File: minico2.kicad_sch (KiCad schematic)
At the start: 36 parts, among them J1 USB_C_Receptacle_USB2.0, J2 GDEY0213Z98, Q1 MMBT2222, Q2 MMBT2222, Q3 IRLML0100TRPBF, U1 ESP32-WROOM-32E, U2 CH340C, U3 TLV62568DBV, U5 SCD30

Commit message: Route PCB
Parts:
- removed C3: 6.8pF, Capacitor_SMD:C_0402_1005Metric, symbol Device:C_Small
- removed U3: TLV62568DBV, Package_TO_SOT_SMD:SOT-23-5, symbol Regulator_Switching:TLV62568DBV
- added H1, H2, H3, H4: MountingHole, MountingHole:MountingHole_2.7mm_M2.5, symbol Mechanical:MountingHole
- added TP1, TP2, TP3: TestPoint_Small, TestPoint:TestPoint_Pad_D2.0mm, symbol Connector:TestPoint_Small
- added TP4, TP5, TP6, TP7: TestPoint_Small, TestPoint:TestPoint_Pad_D1.0mm, symbol Connector:TestPoint_Small
- added U3: AP3418, minico2:SOT-25, symbol minico2:AP3418
- C1: value 10nF -> 100nF; footprint Capacitor_SMD:C_0402_1005Metric -> Capacitor_SMD:C_0603_1608Metric
- C2, C4, C7: footprint Capacitor_SMD:C_0402_1005Metric -> Capacitor_SMD:C_0603_1608Metric
- C9: value 1µF 25F -> 1µF 25V
- L2: footprint Inductor_SMD:L_1008_2520Metric -> Inductor_SMD:L_Taiyo-Yuden_NR-60xx
- R10, R4, R9: footprint Resistor_SMD:R_0402_1005Metric -> Resistor_SMD:R_0603_1608Metric
- R3: value 450kΩ -> 453kΩ; footprint Resistor_SMD:R_0402_1005Metric -> Resistor_SMD:R_0603_1608Metric
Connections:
- net +3V3: now also TP3.1; no longer U2.16 (VCC)
- net +5V: now also U2.16 (VCC), TP2.1, U3.1 (EN), U3.4 (VIN)
- net EN: now also TP5.1
- net ESP_RX: now also TP7.1
- net ESP_TX: now also TP6.1
- net GND: now also TP1.1, U3.2 (GND)
- net GPIO0: now also TP4.1
- net at R3.2, R4.1: now also U3.5 (FB)
- net D+: now reaches J1.A6 (D+), J1.B6 (D+), U2.5 (UD+)
- net D-: now reaches J1.A7 (D-), J1.B7 (D-), U2.6 (UD-)
- net at L1.1: now also U3.3 (SW)
- net ~{RES}: now reaches J2.10 (~{RES})
- net ~{RES}: now also U1.30 (IO18)
- net D/C: now reaches J2.11 (D/C)
- net D/C: now also U1.29 (IO5)
- net ~{CS}: now reaches J2.12 (~{CS})
- net ~{CS}: now also U1.28 (IO17)
- net DISPLAY_SCL: now reaches J2.13 (SCL)
- net DISPLAY_SCL: now also U1.27 (IO16)
- net DISPLAY_SDA: now reaches J2.14 (SDA)
- net DISPLAY_SDA: now also U1.26 (IO4)
- net BUSY: now reaches J2.9 (BUSY)
- net BUSY: now also U1.31 (IO19)
- net SCL renamed SCD30_SCL
- net SDA renamed SCD30_SDA
- net VCOM: no longer names the net of C15.1, J2.24 (VCOM)
- no-connect marks 10 -> 33

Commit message: Ready for 1st production run
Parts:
- C6: footprint Capacitor_SMD:C_0402_1005Metric -> Capacitor_SMD:C_0603_1608Metric
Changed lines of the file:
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@@
       (effects (font (size 1.27 1.27)) (justify left))
     )
-    (property "Footprint" "Capacitor_SMD:C_0402_1005Metric" (id 2) (at 240.03 41.91 0)
+    (property "Footprint" "Capacitor_SMD:C_0603_1608Metric" (id 2) (at 240.03 41.91 0)
       (effects (font (size 1.27 1.27)) hide)
     )
@@
     )
     (path "/ec50315c-196b-4897-bb3e-4d72922deae7"
-      (reference "C6") (unit 1) (value "4.7µF 25V") (footprint "Capacitor_SMD:C_0402_1005Metric")
+      (reference "C6") (unit 1) (value "4.7µF 25V") (footprint "Capacitor_SMD:C_0603_1608Metric")
     )
     (path "/9446568d-cf66-47a7-9c8e-1fd937df18e0"

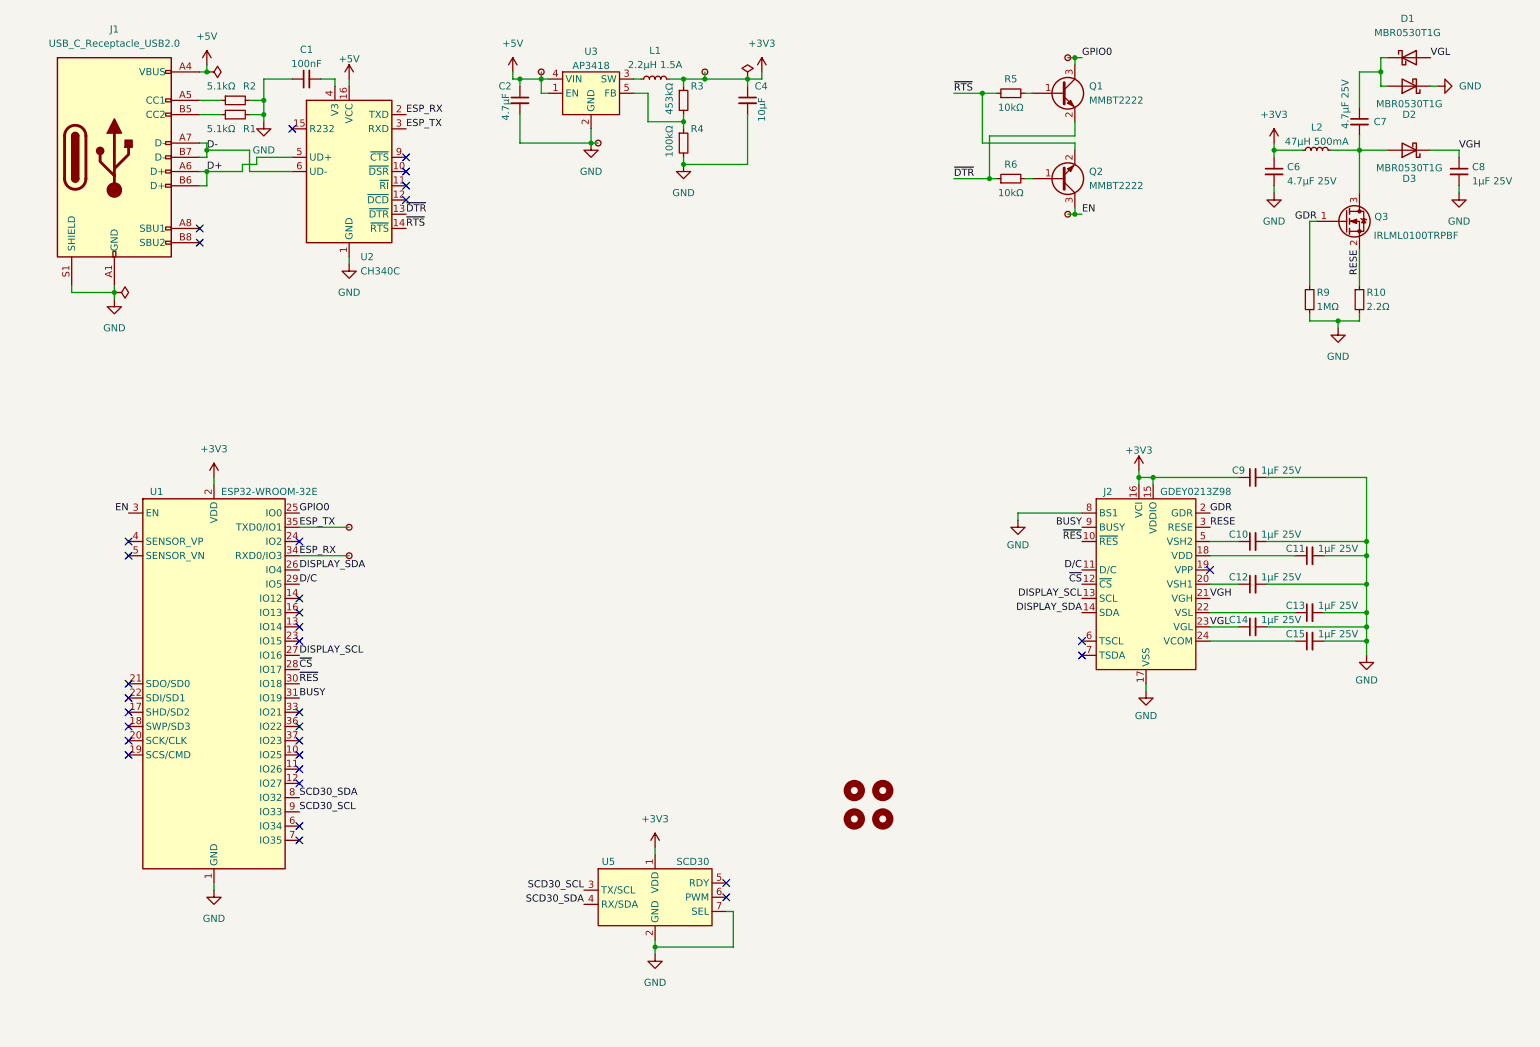
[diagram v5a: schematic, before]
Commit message: Start work on battery version
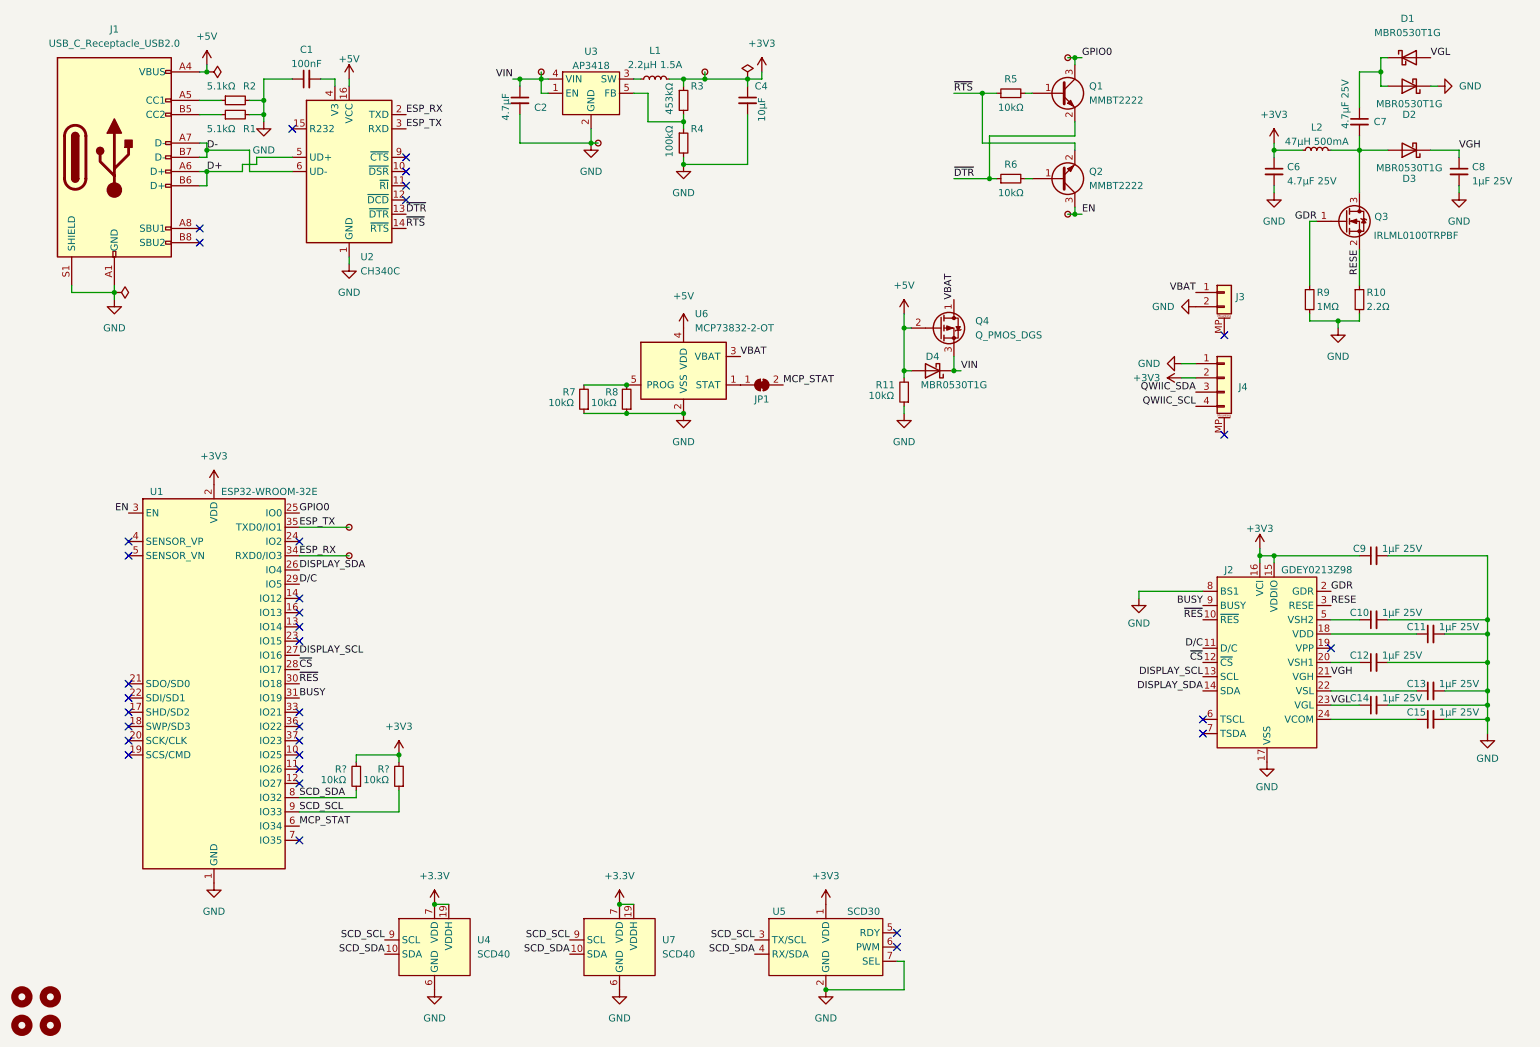
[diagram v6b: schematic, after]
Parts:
- added D4: MBR0530T1G, Diode_SMD:D_SOD-123, symbol Diode:MBR0530
- added J3: Conn_01x02_MountingPin, Connector_JST:JST_PH_S2B-PH-SM4-TB_1x02-1MP_P2.00mm_Horizontal, symbol Connector_Generic_MountingPin:Conn_01x02_MountingPin
- added J4: Conn_01x04_MountingPin, Connector_JST:JST_SH_SM04B-SRSS-TB_1x04-1MP_P1.00mm_Horizontal, symbol Connector_Generic_MountingPin:Conn_01x04_MountingPin
- added JP1: SolderJumper_2_Bridged, Jumper:SolderJumper-2_P1.3mm_Bridged_RoundedPad1.0x1.5mm, symbol Jumper:SolderJumper_2_Bridged
- added Q4: Q_PMOS_DGS, symbol Device:Q_PMOS_DGS
- added R11, R7, R8, R? (x2): 10kΩ, Resistor_SMD:R_0603_1608Metric, symbol Device:R_Small
- added U4, U7: SCD40, minico2:SCD4x, symbol minico2:SCD40
- added U6: MCP73832-2-OT, Package_TO_SOT_SMD:SOT-23-5, symbol Battery_Management:MCP73832-2-OT
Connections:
- net +3V3: now also J4.2 (Pin_2), R?.2, R?.2
- net +5V: now also D4.2 (A), Q4.2 (G), R11.2, U6.4 (VDD); no longer C2.1, TP2.1, U3.1 (EN), U3.4 (VIN)
- net GND: now also J3.2 (Pin_2), J4.1 (Pin_1), R11.1, R7.1, R8.1, U4.20 (GND), U4.21 (GND), U4.6 (GND), U6.2 (VSS), U7.20 (GND), U7.21 (GND), U7.6 (GND)
- net MCP_STAT: now reaches U1.6 (IO34)
- net MCP_STAT: now also JP1.2 (B)
- net SCD30_SCL renamed SCD_SCL
- net SCD_SCL: now also R?.1, U4.9 (SCL), U7.9 (SCL)
- net SCD30_SDA renamed SCD_SDA
- net SCD_SDA: now also R?.1, U4.10 (SDA), U7.10 (SDA)
- new net: R7.2, R8.2, U6.5 (PROG)
- new net: JP1.1 (A), U6.1 (STAT)
- new net +3.3V: U4.19 (VDDH), U4.7 (VDD), U7.19 (VDDH), U7.7 (VDD)
- new net QWIIC_SCL: J4.4 (Pin_4)
- new net QWIIC_SDA: J4.3 (Pin_3)
- new net VBAT: J3.1 (Pin_1), Q4.1 (D), U6.3 (VBAT)
- new net VIN: C2.1, D4.1 (K), Q4.3 (S), TP2.1, U3.1 (EN), U3.4 (VIN)
- no-connect marks 33 -> 34
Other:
- moved on the sheet: C10, C11, C12, C13, C14, C15, C9, J2, U5
